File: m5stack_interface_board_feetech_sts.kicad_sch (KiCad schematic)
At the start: 13 parts, among them J2 BAT, J3 Conn_01x04, J4 0022057035, Q1 2SA1162, U1 MAX3485, U2 AP7384-33SA

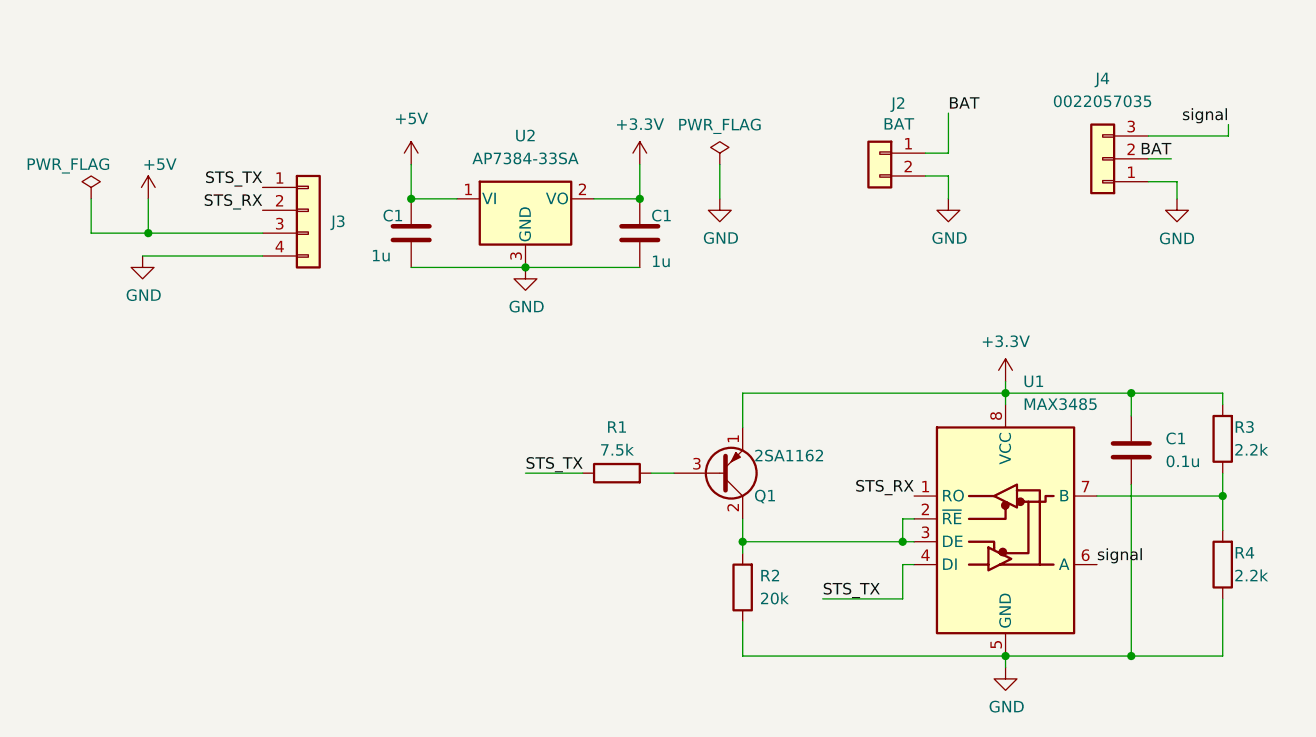
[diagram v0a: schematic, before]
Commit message: complete to design ver. double molex (#1)
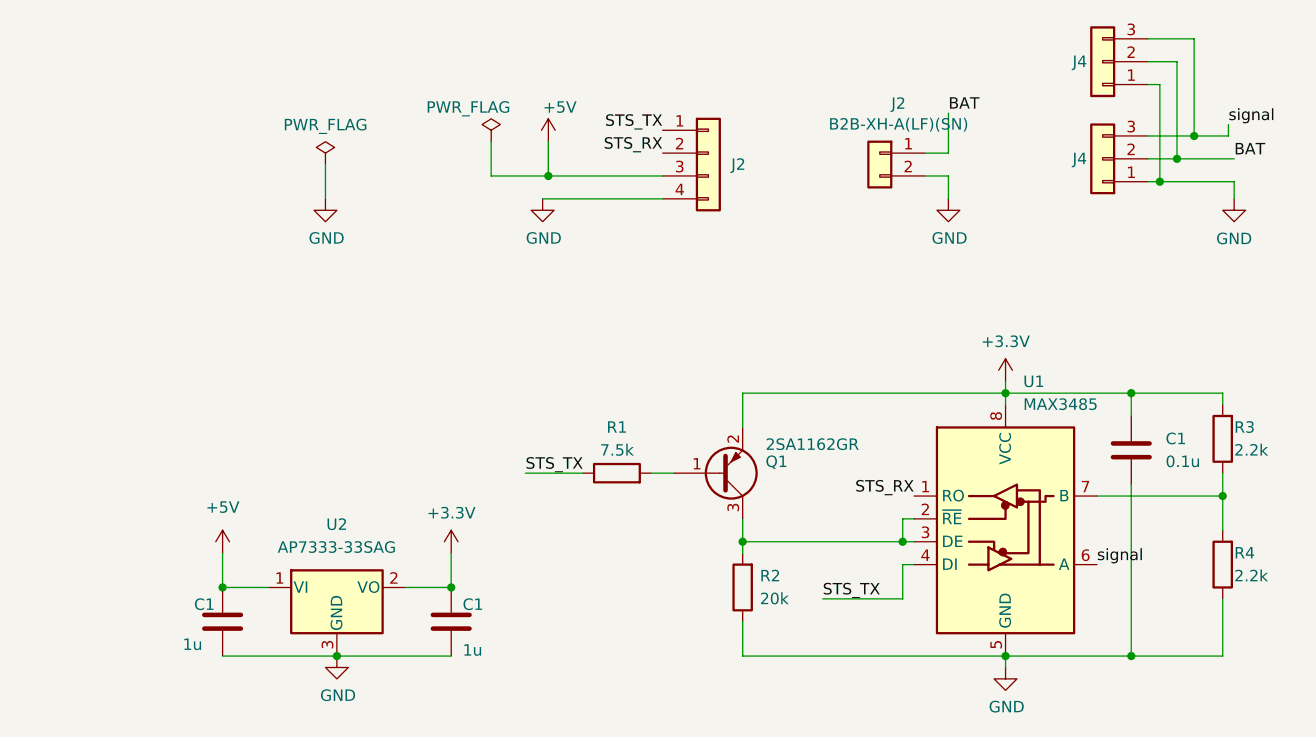
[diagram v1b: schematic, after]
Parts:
- removed Q1: 2SA1162, Package_TO_SOT_SMD:SC-59_Handsoldering, symbol Transistor_BJT:2SA1015
- added J4: 22035035, Connector_Molex:Molex_SPOX_5267-03A_1x03_P2.50mm_Vertical, symbol Connector_Generic:Conn_01x03
- added Q1: 2SA1162GR, Package_TO_SOT_SMD:SC-59_Handsoldering, symbol bsl_symbols:2SA1162
- J2: value BAT -> B2B-XH-A(LF)(SN); footprint Connector_JST:JST_XH_S2B-XH-A_1x02_P2.50mm_Horizontal -> Connector_JST:JST_XH_B2B-XH-A_1x02_P2.50mm_Vertical
- J2: renamed from J3; value Conn_01x04 -> B4B-PH-K-S(LF)(SN); footprint Connector_JST:JST_PH_S4B-PH-K_1x04_P2.00mm_Horizontal -> Connector_JST:JST_PH_B4B-PH-K_1x04_P2.00mm_Vertical
- J4: value 0022057035 -> 22035035; footprint Connector_Molex:Molex_SPOX_5268-03A_1x03_P2.50mm_Horizontal -> Connector_Molex:Molex_SPOX_5267-03A_1x03_P2.50mm_Vertical
- U1: footprint Package_SO:SOP-8_5.28x5.23mm_P1.27mm -> Package_SO:SOP-8_3.9x4.9mm_P1.27mm
- U2: value AP7384-33SA -> AP7333-33SAG
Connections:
- net +3.3V: now also Q1.2 (E)
- net BAT: now also J4.2 (Pin_2)
- net GND: now also J4.1 (Pin_1)
- net signal: now also J4.3 (Pin_3)
- net at R2.2, U1.2 (~{RE}), U1.3 (DE): now also Q1.3 (C)
- net at R1.2: now also Q1.1 (B)
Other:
- moved on the sheet: C1, J2, U2
